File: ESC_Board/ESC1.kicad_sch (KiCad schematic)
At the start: 47 parts, among them Q10 SIR182DP, Q11 SIR182Dp, Q12 SIR182DP, Q13 SIR182DP, Q14 SIR182DP, Q2 AO3400A, Q9 SIR182DP, U7 STM32F051K8Ux, U8 DRV8300DRGER, U9 INA180A1

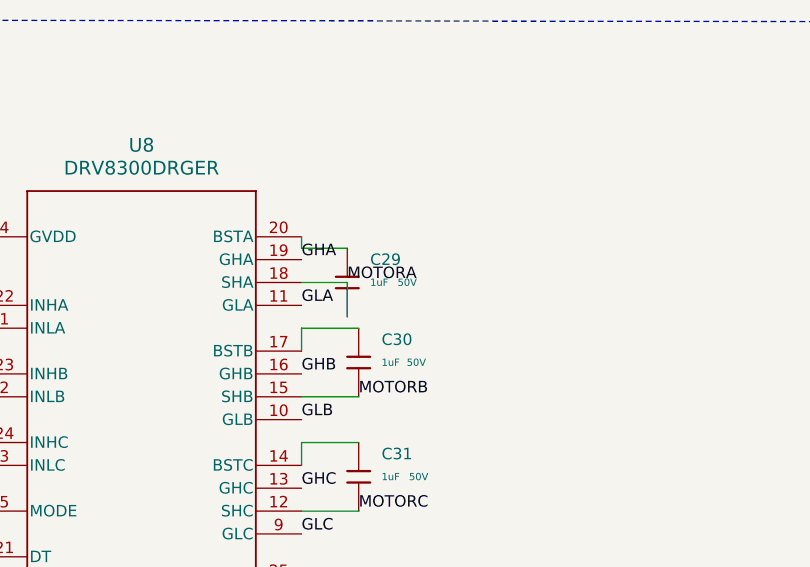
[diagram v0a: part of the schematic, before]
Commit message: ESC Board: Major overhauls to schematic, preliminary layout
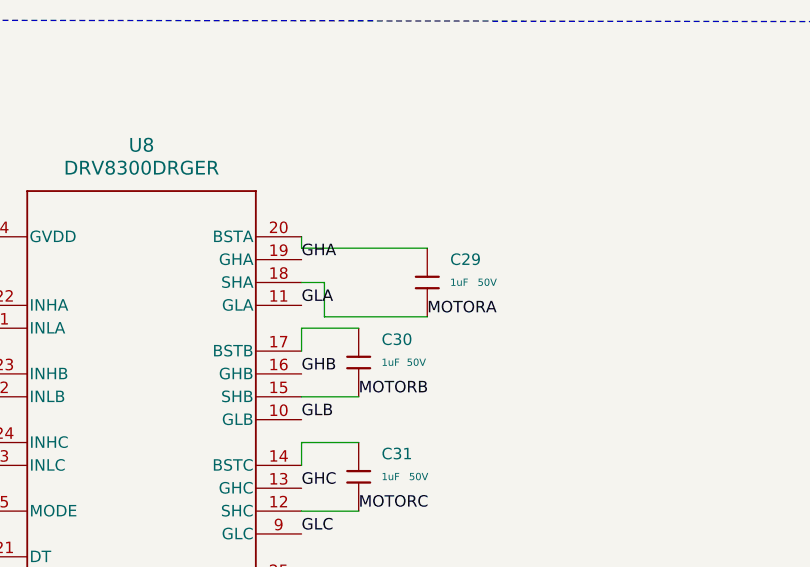
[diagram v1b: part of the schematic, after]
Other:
- moved on the sheet: C29
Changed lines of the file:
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@@
-	(wire
-		(pts
-			(xy 105.41 128.27) (xy 100.33 128.27)
-		)
-		(stroke
-			(width 0)
-			(type default)
-		)
-	)
 	(wire
 		(pts
@@
 	(wire
 		(pts
+			(xy 102.87 132.08) (xy 102.87 128.27)
+		)
+		(stroke
+			(width 0)
+			(type default)
+		)
+	)
+	(wire
+		(pts
 			(xy 76.2 76.2) (xy 81.28 76.2)
 		)
@@
 	(wire
 		(pts
+			(xy 102.87 128.27) (xy 100.33 128.27)
+		)
+		(stroke
+			(width 0)
+			(type default)
+		)
+	)
+	(wire
+		(pts
 			(xy 267.97 30.48) (xy 267.97 31.75)
 		)
@@
 	(wire
 		(pts
-			(xy 105.41 132.08) (xy 105.41 128.27)
-		)
-		(stroke
-			(width 0)
-			(type default)
-		)
-	)
-	(wire
-		(pts
 			(xy 114.3 73.66) (xy 111.76 73.66)
 		)
@@
 	(wire
 		(pts
+			(xy 102.87 132.08) (xy 114.3 132.08)
+		)
+		(stroke
+			(width 0)
+			(type default)
+		)
+	)
+	(wire
+		(pts
 			(xy 100.33 161.29) (xy 100.33 166.37)
 		)
@@
 	(wire
 		(pts
-			(xy 100.33 124.46) (xy 105.41 124.46)
+			(xy 100.33 124.46) (xy 114.3 124.46)
 		)
 		(stroke
@@
 	)
 	(label "MOTORA"
-		(at 105.41 128.27 0)
+		(at 114.3 132.08 0)
 		(effects
 			(font
@@
 		(lib_name "0603,1uF_2")
 		(lib_id "PCM_JLCPCB-Capacitors:0603,1uF")
-		(at 105.41 128.27 0)
+		(at 114.3 128.27 0)
 		(unit 1)
 		(exclude_from_sim no)
@@
 		(dnp no)
 		(property "Reference" "C29"
-			(at 107.95 125.7299 0)
+			(at 116.84 125.7299 0)
 			(effects
 				(font
@@
 		)
 		(property "Value" "1uF"
-			(at 107.95 128.27 0)
+			(at 116.84 128.27 0)
 			(effects
 				(font
@@
 		)
 		(property "Footprint" "PCM_JLCPCB:C_0603"
-			(at 103.632 128.27 90)
+			(at 112.522 128.27 90)
 			(effects
 				(font
@@
 		)
 		(property "Datasheet" ""
-			(at 105.41 128.27 0)
+			(at 114.3 128.27 0)
 			(effects
 				(font
@@
 		)
 		(property "Description" "50V 1uF X7R ±10% 0603 Multilayer Ceramic Capacitors MLCC - SMD/SMT ROHS"
-			(at 105.41 128.27 0)
+			(at 114.3 128.27 0)
 			(effects
 				(font
@@
 		)
 		(property "LCSC" "C6119857"
-			(at 105.41 128.27 0)
+			(at 114.3 128.27 0)
 			(effects
 				(font
@@
 		)
 		(property "Stock" "11587280"
-			(at 105.41 128.27 0)
+			(at 114.3 128.27 0)
 			(effects
 				(font
@@
 		)
 		(property "Price" "0.008USD"
-			(at 105.41 128.27 0)
+			(at 114.3 128.27 0)
 			(effects
 				(font
@@
 		)
 		(property "Process" "SMT"
-			(at 105.41 128.27 0)
+			(at 114.3 128.27 0)
 			(effects
 				(font
@@
 		)
 		(property "Minimum Qty" "20"
-			(at 105.41 128.27 0)
+			(at 114.3 128.27 0)
 			(effects
 				(font
@@
 		)
 		(property "Attrition Qty" "10"
-			(at 105.41 128.27 0)
+			(at 114.3 128.27 0)
 			(effects
 				(font
@@
 		)
 		(property "Class" "Basic Component"
-			(at 105.41 128.27 0)
+			(at 114.3 128.27 0)
 			(effects
 				(font
@@
 		)
 		(property "Category" "Capacitors,Multilayer Ceramic Capacitors MLCC - SMD/SMT"
-			(at 105.41 128.27 0)
+			(at 114.3 128.27 0)
 			(effects
 				(font
@@
 		)
 		(property "Manufacturer" ""
-			(at 105.41 128.27 0)
+			(at 114.3 128.27 0)
 			(effects
 				(font
@@
 		)
 		(property "Part" ""
-			(at 105.41 128.27 0)
+			(at 114.3 128.27 0)
 			(effects
 				(font
@@
 		)
 		(property "Voltage Rated" "50V"
-			(at 110.998 128.27 0)
+			(at 119.888 128.27 0)
 			(effects
 				(font
@@
 		)
 		(property "Tolerance" "±10%"
-			(at 105.41 128.27 0)
+			(at 114.3 128.27 0)
 			(effects
 				(font
@@
 		)
 		(property "Capacitance" "1uF"
-			(at 105.41 128.27 0)
+			(at 114.3 128.27 0)
 			(effects
 				(font
@@
 		)
 		(property "Temperature Coefficient" "X5R"
-			(at 105.41 128.27 0)
-			(effects
-				(font
+			(at 114.3 128.27 0)
+			(effects
+				(font
